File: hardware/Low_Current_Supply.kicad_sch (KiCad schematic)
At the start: 0 parts

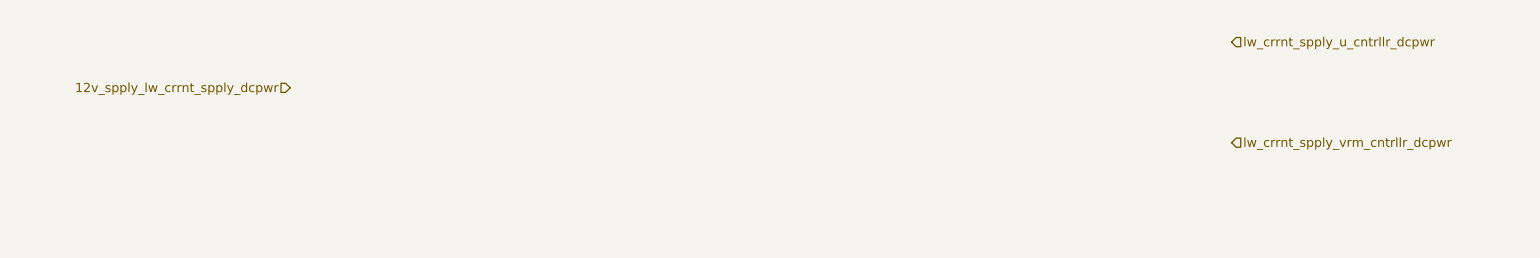
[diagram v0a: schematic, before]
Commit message: feat(schematic): initial low current supply
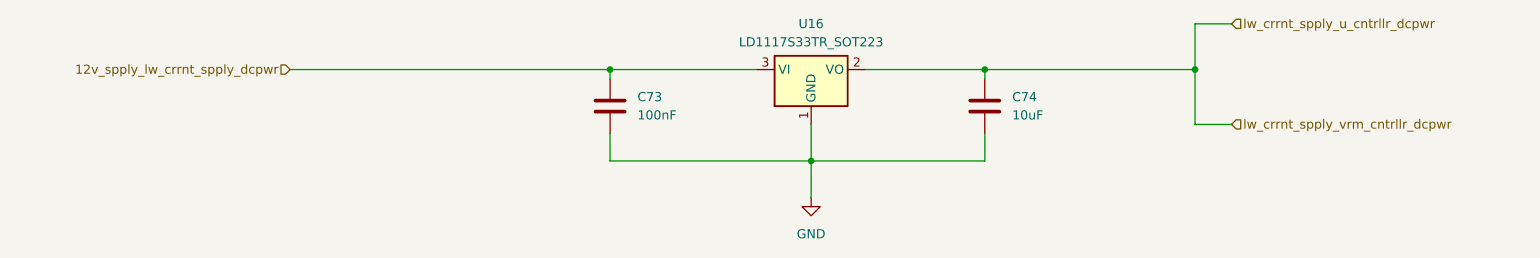
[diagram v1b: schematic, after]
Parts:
- added C73: 100nF, symbol Device:C
- added C74: 10uF, symbol Device:C
- added U16: LD1117S33TR_SOT223, Package_TO_SOT_SMD:SOT-223-3_TabPin2, symbol Regulator_Linear:LD1117S33TR_SOT223
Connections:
- net 12v_spply_lw_crrnt_spply_dcpwr: now also C73.1, U16.3 (VI)
- net lw_crrnt_spply_u_cntrllr_dcpwr: now also C74.1, U16.2 (VO)
- new net GND: C73.2, C74.2, U16.1 (GND)

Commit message: chore: update project references
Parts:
- renumbered C73 to C5001, C74 to C5002, U16 to U5001
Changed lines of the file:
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@@
 		(dnp no)
 		(fields_autoplaced yes)
-		(property "Reference" "#PWR035"
+		(property "Reference" "#PWR05001"
 			(at 144.78 114.3 0)
 			(effects
@@
 			(project ""
 				(path "/d5303413-7068-41ba-88e3-39dfa38d31b7/c1da4524-645b-40e4-93f8-f7b345299022"
-					(reference "#PWR035")
+					(reference "#PWR05001")
 					(unit 1)
 				)
@@
 		(dnp no)
 		(fields_autoplaced yes)
-		(property "Reference" "C73"
+		(property "Reference" "C5001"
 			(at 120.65 93.9799 0)
 			(effects
@@
 			(project ""
 				(path "/d5303413-7068-41ba-88e3-39dfa38d31b7/c1da4524-645b-40e4-93f8-f7b345299022"
-					(reference "C73")
+					(reference "C5001")
 					(unit 1)
 				)
@@
 		(dnp no)
 		(fields_autoplaced yes)
-		(property "Reference" "U16"
+		(property "Reference" "U5001"
 			(at 144.78 83.82 0)
 			(effects
@@
 			(project ""
 				(path "/d5303413-7068-41ba-88e3-39dfa38d31b7/c1da4524-645b-40e4-93f8-f7b345299022"
-					(reference "U16")
+					(reference "U5001")
 					(unit 1)
 				)
@@
 		(dnp no)
 		(fields_autoplaced yes)
-		(property "Reference" "C74"
+		(property "Reference" "C5002"
 			(at 172.72 93.9799 0)
 			(effects
@@
 			(project "gpu-external-power-supply"
 				(path "/d5303413-7068-41ba-88e3-39dfa38d31b7/c1da4524-645b-40e4-93f8-f7b345299022"
-					(reference "C74")
-					(unit 1)
-				)
+					(reference "C5002")
+					(unit 1)
+				)

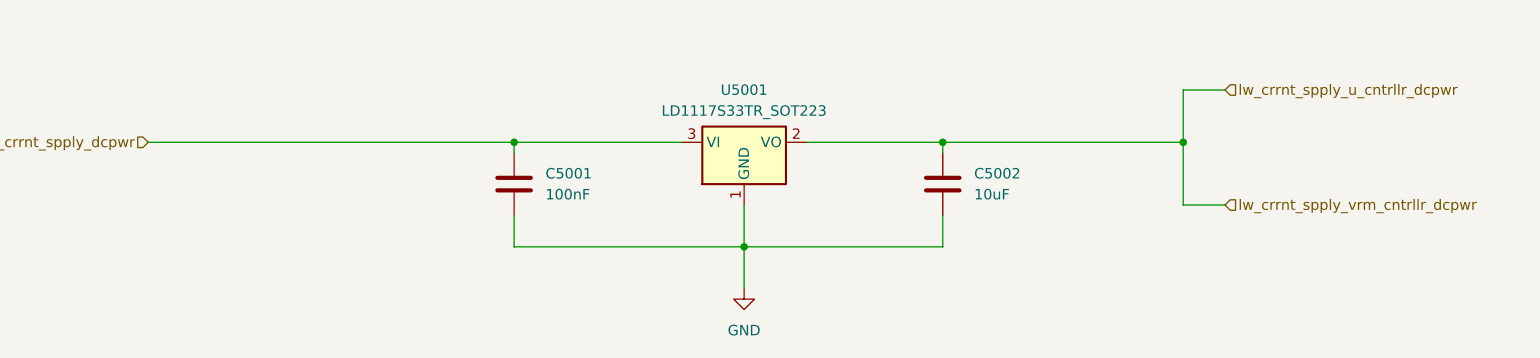
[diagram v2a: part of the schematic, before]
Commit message: feat(12v): add correct sensor
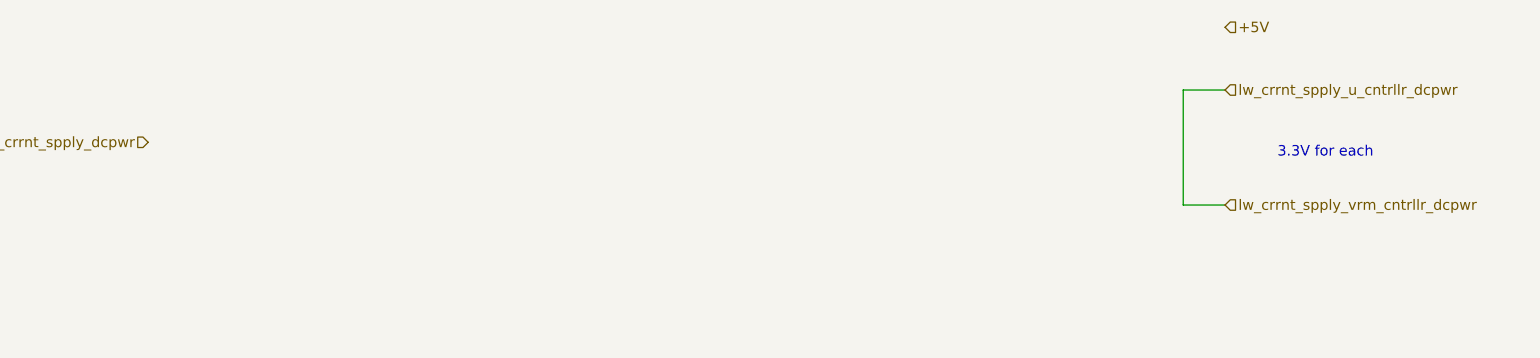
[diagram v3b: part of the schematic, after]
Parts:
- removed C5001: 100nF, symbol Device:C
- removed C5002: 10uF, symbol Device:C
- removed U5001: LD1117S33TR_SOT223, Package_TO_SOT_SMD:SOT-223-3_TabPin2, symbol Regulator_Linear:LD1117S33TR_SOT223
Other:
- note added: "3.3V for each"

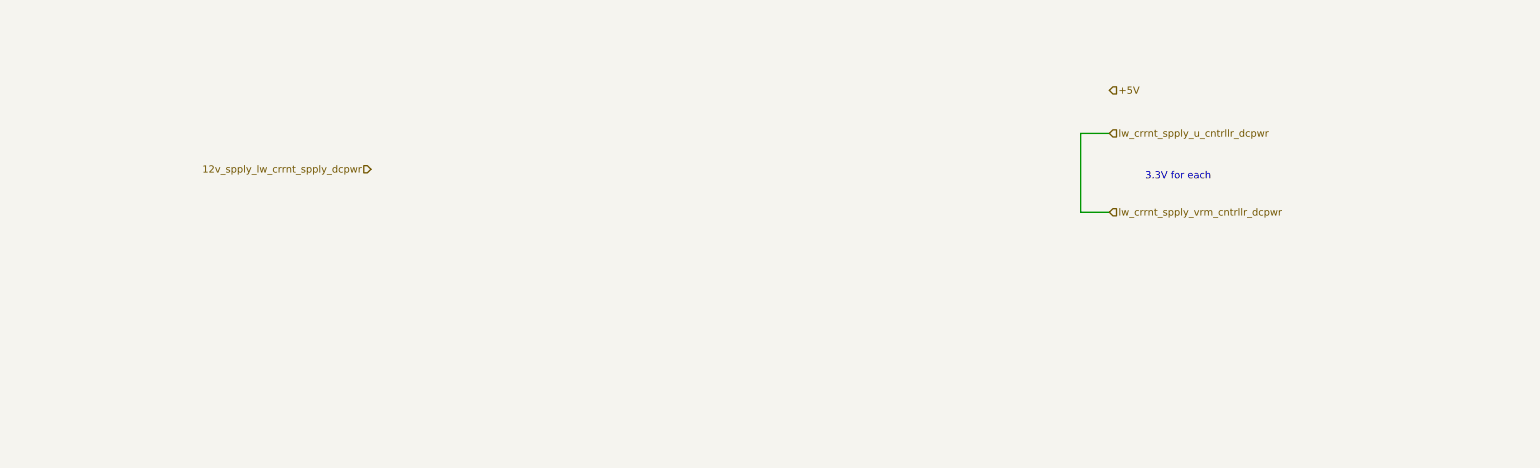
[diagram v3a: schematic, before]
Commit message: fix(schematic): 12V Supply & Low Current Supply
Added proper switching 5V and linear 3.3V ICs.
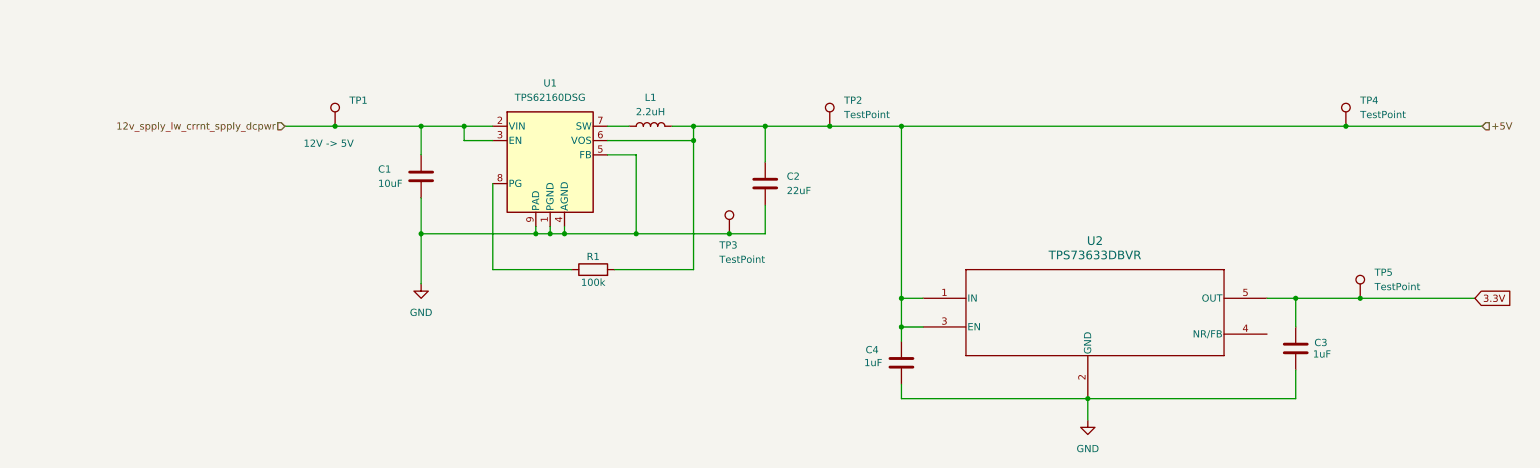
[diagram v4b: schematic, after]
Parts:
- added C1: 10uF, Capacitor_SMD:C_0805_2012Metric_Pad1.18x1.45mm_HandSolder, symbol Device:C
- added C2: 22uF, symbol Device:C
- added C3, C4: 1uF, symbol Device:C
- added L1: 2.2uH, symbol Device:L
- added R1: 100k, symbol Device:R
- added TP1: 12V -> 5V, symbol Connector:TestPoint
- added TP2, TP3, TP4, TP5: TestPoint, symbol Connector:TestPoint
- added U1: TPS62160DSG, Package_SON:WSON-8-1EP_2x2mm_P0.5mm_EP0.9x1.6mm_ThermalVias, symbol Regulator_Switching:TPS62160DSG
- added U2: TPS73633DBVR, DBV5, symbol TPS73233DBVR:TPS73633DBVR
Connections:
- net +5V : now also C2.1, C4.1, L1.2, R1.2, TP2.1, TP4.1, U1.6 (VOS), U2.1 (IN), U2.3 (EN)
- net 12v_spply_lw_crrnt_spply_dcpwr: now also C1.1, TP1.1, U1.2 (VIN), U1.3 (EN)
- new net: L1.1, U1.7 (SW)
- new net: R1.1, U1.8 (PG)
- new net 3.3V: C3.1, TP5.1, U2.5 (OUT)
- new net GND: C1.2, C2.2, C3.2, C4.2, TP3.1, U1.1 (PGND), U1.4 (AGND), U1.5 (FB), U1.9 (PAD), U2.2 (GND)
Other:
- note removed: "3.3V for each"

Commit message: feat(schematic): 12V and Low Current
Final changes: Added test points and assigned all footprints.
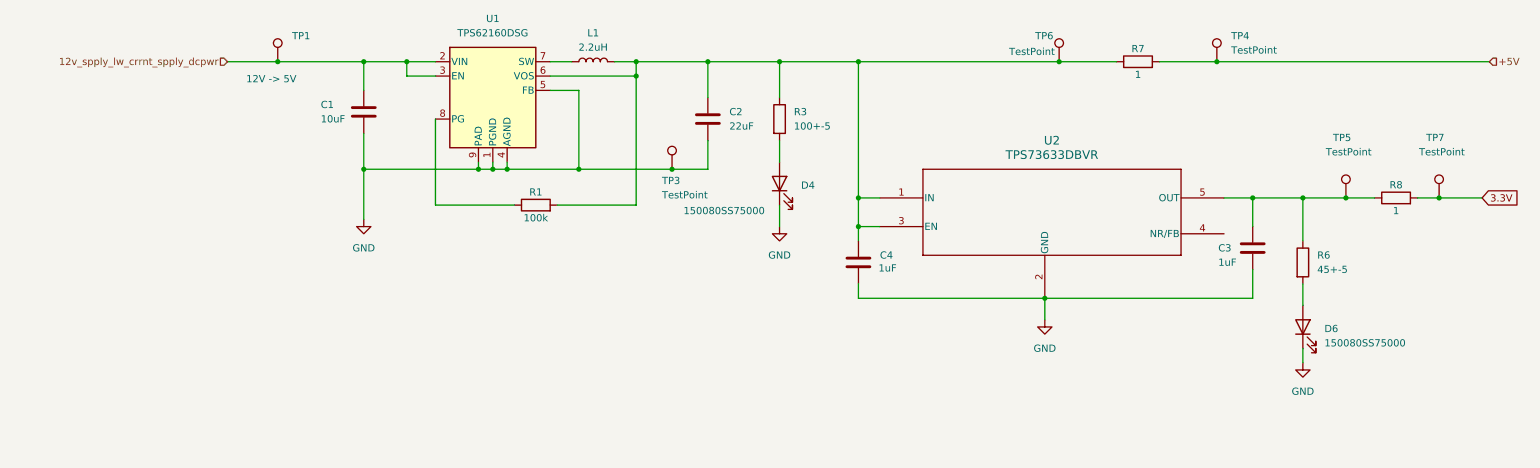
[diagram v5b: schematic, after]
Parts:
- removed TP2: TestPoint, symbol Connector:TestPoint
- added D4, D6: 150080SS75000, LED_SMD:LED_0805_2012Metric_Pad1.15x1.40mm_HandSolder, symbol Device:LED
- added R3: 100+-5, Resistor_SMD:R_0805_2012Metric, symbol Device:R
- added R6: 45+-5, Resistor_SMD:R_0805_2012Metric, symbol Device:R
- added R7, R8: 1, Resistor_SMD:R_0805_2012Metric, symbol Device:R
- added TP6, TP7: TestPoint, TestPoint:TestPoint_Pad_2.0x2.0mm, symbol Connector:TestPoint
- C2, C3, C4: footprint (none) -> Capacitor_SMD:C_0805_2012Metric
- L1: footprint (none) -> Inductor_SMD:L_0805_2012Metric_Pad1.15x1.40mm_HandSolder
- R1: footprint (none) -> Resistor_SMD:R_0805_2012Metric
- TP1, TP3, TP4, TP5: footprint (none) -> TestPoint:TestPoint_Pad_2.0x2.0mm
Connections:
- net +5V : now also R7.2; no longer C2.1, C4.1, L1.2, R1.2, U1.6 (VOS), U2.1 (IN), U2.3 (EN)
- net 3.3V: now also R8.2, TP7.1; no longer C3.1, TP5.1, U2.5 (OUT)
- net GND: now also D4.1 (K), D6.1 (K)
- new net: C3.1, R6.1, R8.1, TP5.1, U2.5 (OUT)
- new net: C2.1, C4.1, L1.2, R1.2, R3.1, R7.1, TP6.1, U1.6 (VOS), U2.1 (IN), U2.3 (EN)
- new net: D6.2 (A), R6.2
- new net: D4.2 (A), R3.2
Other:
- moved on the sheet: C1, C2, C3, C4, L1, R1, TP1, TP3, TP4, TP5, U1, U2

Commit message: feat(schematic): footprints
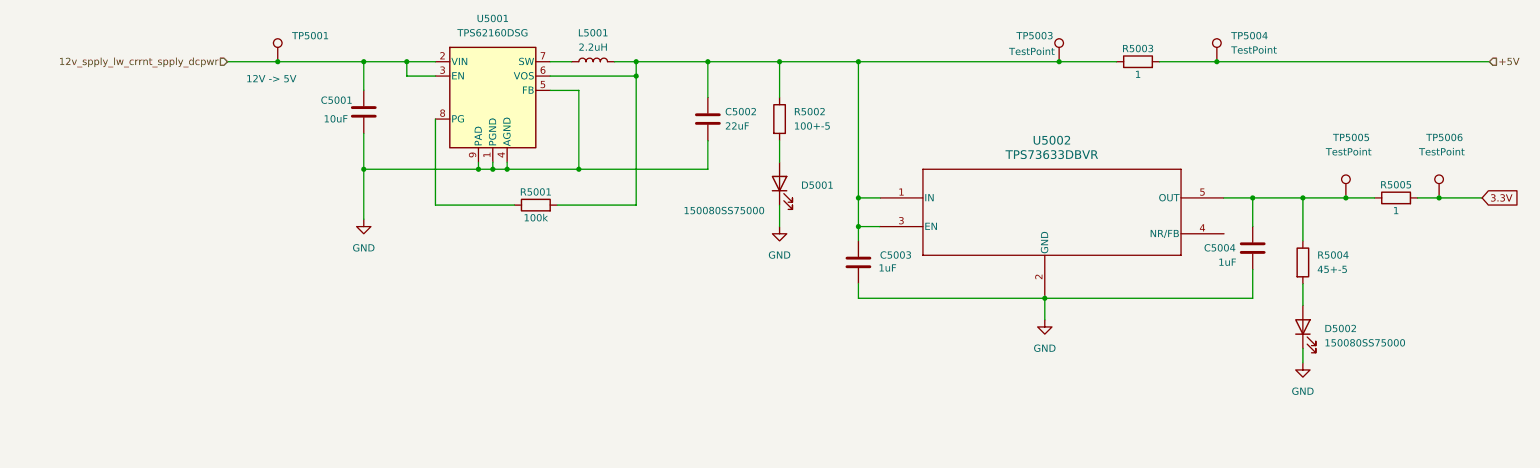
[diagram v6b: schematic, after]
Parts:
- removed TP3: TestPoint, TestPoint:TestPoint_Pad_2.0x2.0mm, symbol Connector:TestPoint
- TP5001: renamed from TP1; footprint TestPoint:TestPoint_Pad_2.0x2.0mm -> TestPoint:TestPoint_Pad_1.5x1.5mm
- TP5003: renamed from TP6; footprint TestPoint:TestPoint_Pad_2.0x2.0mm -> TestPoint:TestPoint_Pad_1.5x1.5mm
- TP5004: renamed from TP4; footprint TestPoint:TestPoint_Pad_2.0x2.0mm -> TestPoint:TestPoint_Pad_1.5x1.5mm
- TP5005: renamed from TP5; footprint TestPoint:TestPoint_Pad_2.0x2.0mm -> TestPoint:TestPoint_Pad_1.5x1.5mm
- TP5006: renamed from TP7; footprint TestPoint:TestPoint_Pad_2.0x2.0mm -> TestPoint:TestPoint_Pad_1.5x1.5mm
- U5002: renamed from U2; footprint DBV5 -> TPS73633DBVR_SOT23-5:DBV5
- renumbered C1 to C5001, C2 to C5002, C4 to C5003, C3 to C5004, D4 to D5001, D6 to D5002, L1 to L5001, R1 to R5001, R3 to R5002, R7 to R5003, R6 to R5004, R8 to R5005, U1 to U5001

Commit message: chore: update annotations
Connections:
- net +5V  renamed 5V
- net 12v_spply_lw_crrnt_spply_dcpwr renamed 12V
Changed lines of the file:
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@@
+		)
+	)
+	(global_label "5V"
+		(shape input)
+		(at 270.51 71.12 0)
+		(fields_autoplaced yes)
+		(effects
+			(font
+				(size 1.27 1.27)
+			)
+			(justify left)
+		)
+		(property "Intersheetrefs" "${INTERSHEET_REFS}"
+			(at 275.7933 71.12 0)
+			(effects
+				(font
+					(size 1.27 1.27)
+				)
+				(justify left)
+				(hide yes)
+			)
+		)
+	)
+	(global_label "12V"
+		(shape input)
+		(at 46.99 71.12 180)
+		(fields_autoplaced yes)
+		(effects
+			(font
+				(size 1.27 1.27)
+			)
+			(justify right)
+		)
+		(property "Intersheetrefs" "${INTERSHEET_REFS}"
+			(at 40.4972 71.12 0)
+			(effects
+				(font
+					(size 1.27 1.27)
+				)
+				(justify right)
+				(hide yes)
+			)
 		)
 	)
@@
 		)
 	)
-	(hierarchical_label "12v_spply_lw_crrnt_spply_dcpwr"
-		(shape input)
-		(at 46.99 71.12 180)
-		(fields_autoplaced yes)
-		(effects
-			(font
-				(size 1.27 1.27)
-			)
-			(justify right)
-		)
-	)
-	(hierarchical_label "+5V "
-		(shape input)
-		(at 270.51 71.12 0)
-		(fields_autoplaced yes)
-		(effects
-			(font
-				(size 1.27 1.27)
-			)
-			(justify left)
-		)
-	)

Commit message: feat(PCB): fix all DRC errors
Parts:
- U5002: footprint TPS73633DBVR_SOT23-5:DBV5 -> Package_TO_SOT_SMD:SOT-23-5
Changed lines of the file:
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@@
 			)
 		)
-		(property "Footprint" "TPS73633DBVR_SOT23-5:DBV5"
+		(property "Footprint" "Package_TO_SOT_SMD:SOT-23-5"
 			(at 174.498 87.63 0)
 			(effects
